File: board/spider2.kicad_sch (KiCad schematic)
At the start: 100 parts, among them J1 NRJ6HH, J10 PJ-320A, J11 PJ359, J12 PJ359, J13 PJ359, J14 PJ359, J15 PJ359, J16 PJ359, J19 PJ359, J2 NRJ6HH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

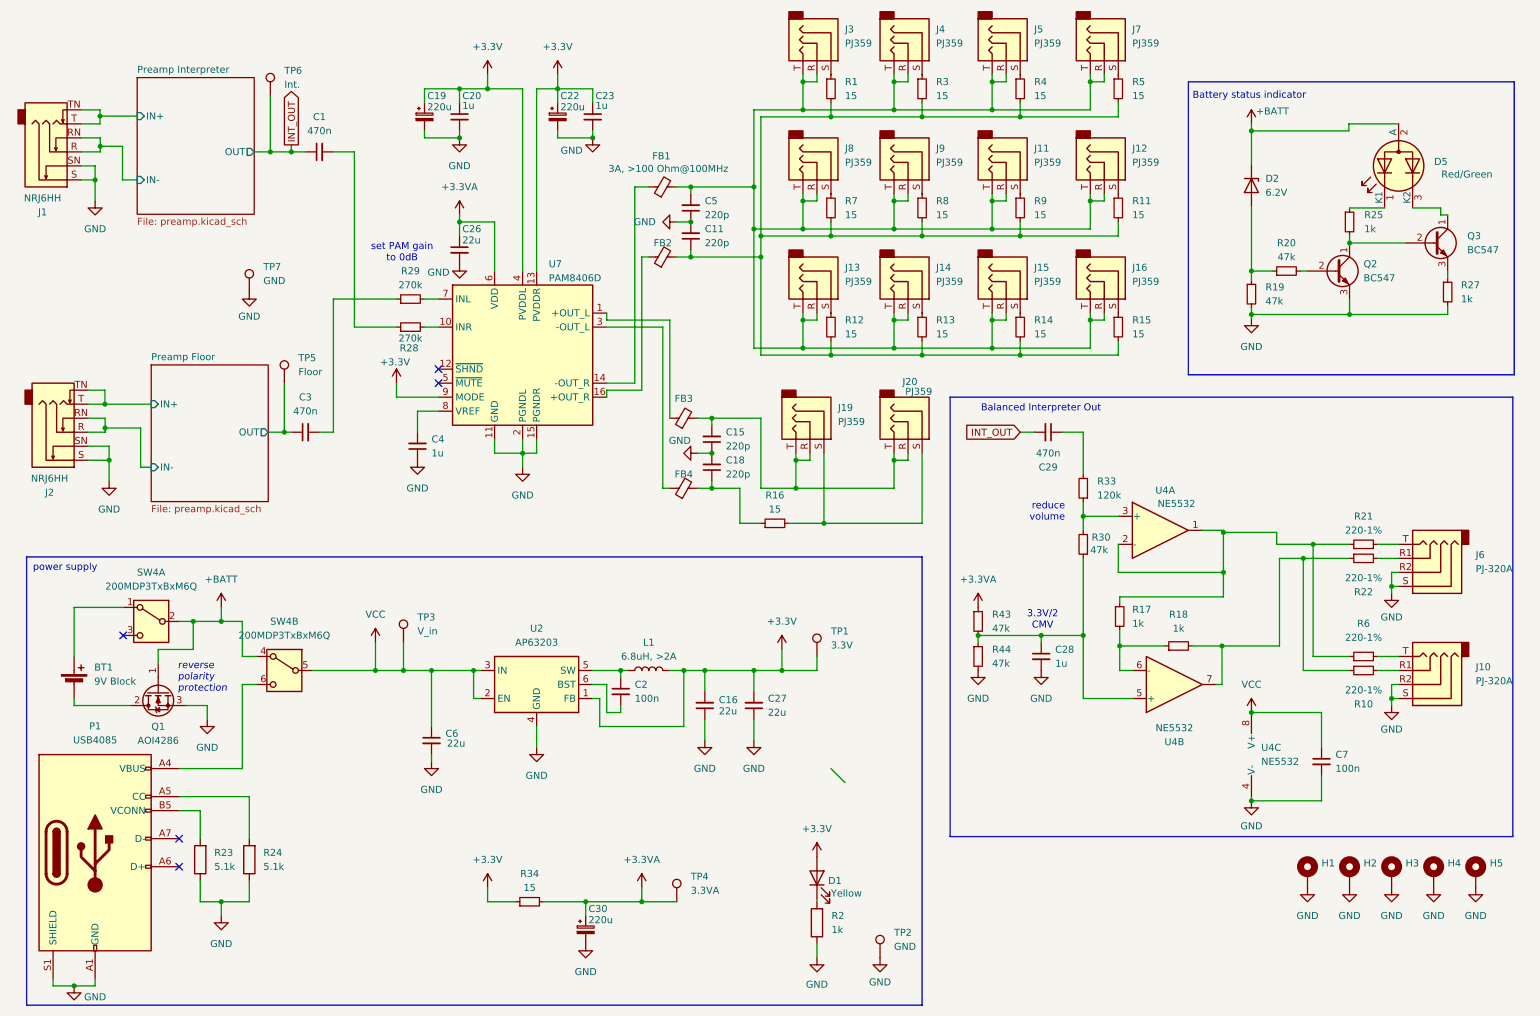
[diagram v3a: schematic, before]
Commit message: reduce BOM and more mechanical stable PJ358
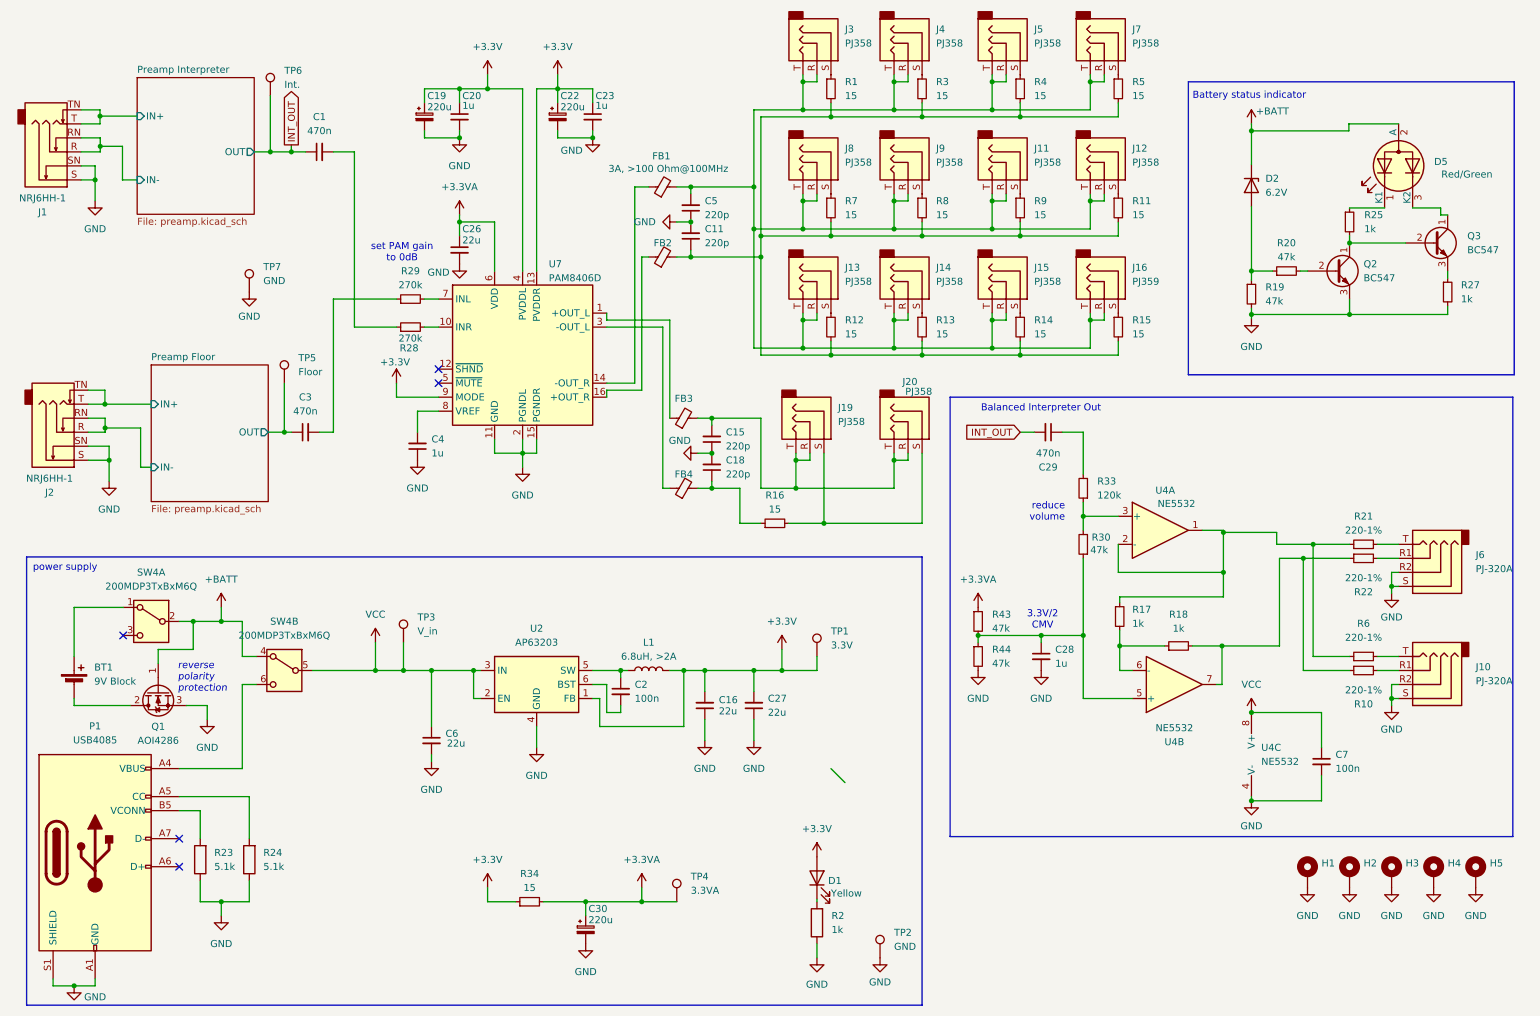
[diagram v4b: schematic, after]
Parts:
- J1, J2: value NRJ6HH -> NRJ6HH-1
- J11, J12, J13, J14, J15, J19, J20, J3, J4, J5, J7, J8, J9: value PJ359 -> PJ358
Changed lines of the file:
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@@
 			)
 		)
-		(property "Value" "PJ359"
+		(property "Value" "PJ358"
 			(at 162.56 64.1349 90)
 			(effects
@@
 			)
 		)
-		(property "Value" "PJ359"
+		(property "Value" "PJ358"
 			(at 162.56 20.9549 90)
 			(effects
@@
 			)
 		)
-		(property "Value" "PJ359"
+		(property "Value" "PJ358"
 			(at 214.63 20.9549 90)
 			(effects
@@
 			)
 		)
-		(property "Value" "PJ359"
+		(property "Value" "PJ358"
 			(at 196.85 64.1349 90)
 			(effects
@@
 			)
 		)
-		(property "Value" "PJ359"
+		(property "Value" "PJ358"
 			(at 161.29 89.5349 90)
 			(effects
@@
 			)
 		)
-		(property "Value" "PJ359"
+		(property "Value" "PJ358"
 			(at 196.85 42.5449 90)
 			(effects
@@
 			)
 		)
-		(property "Value" "NRJ6HH"
+		(property "Value" "NRJ6HH-1"
 			(at 18.415 99.822 0)
 			(effects
@@
 			)
 		)
-		(property "Value" "PJ359"
+		(property "Value" "PJ358"
 			(at 179.07 20.9549 90)
 			(effects
@@
 			)
 		)
-		(property "Value" "PJ359"
+		(property "Value" "PJ358"
 			(at 173.482 84.074 90)
 			(effects
@@
 			)
 		)
-		(property "Value" "NRJ6HH"
+		(property "Value" "NRJ6HH-1"
 			(at 17.145 49.022 0)
 			(effects
@@
 			)
 		)
-		(property "Value" "PJ359"
+		(property "Value" "PJ358"
 			(at 214.63 42.5449 90)
 			(effects
@@
 			)
 		)
-		(property "Value" "PJ359"
+		(property "Value" "PJ358"
 			(at 179.07 42.5449 90)
 			(effects
@@
 			)
 		)
-		(property "Value" "PJ359"
+		(property "Value" "PJ358"
 			(at 196.85 20.9549 90)
 			(effects
@@
 			)
 		)
-		(property "Value" "PJ359"
+		(property "Value" "PJ358"
 			(at 162.56 42.5449 90)
 			(effects
@@
 			)
 		)
-		(property "Value" "PJ359"
+		(property "Value" "PJ358"
 			(at 179.07 64.1349 90)
 			(effects

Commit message: incoorperate matthias feedback
- clearances
- opamp swap
- shorter traces
- ...
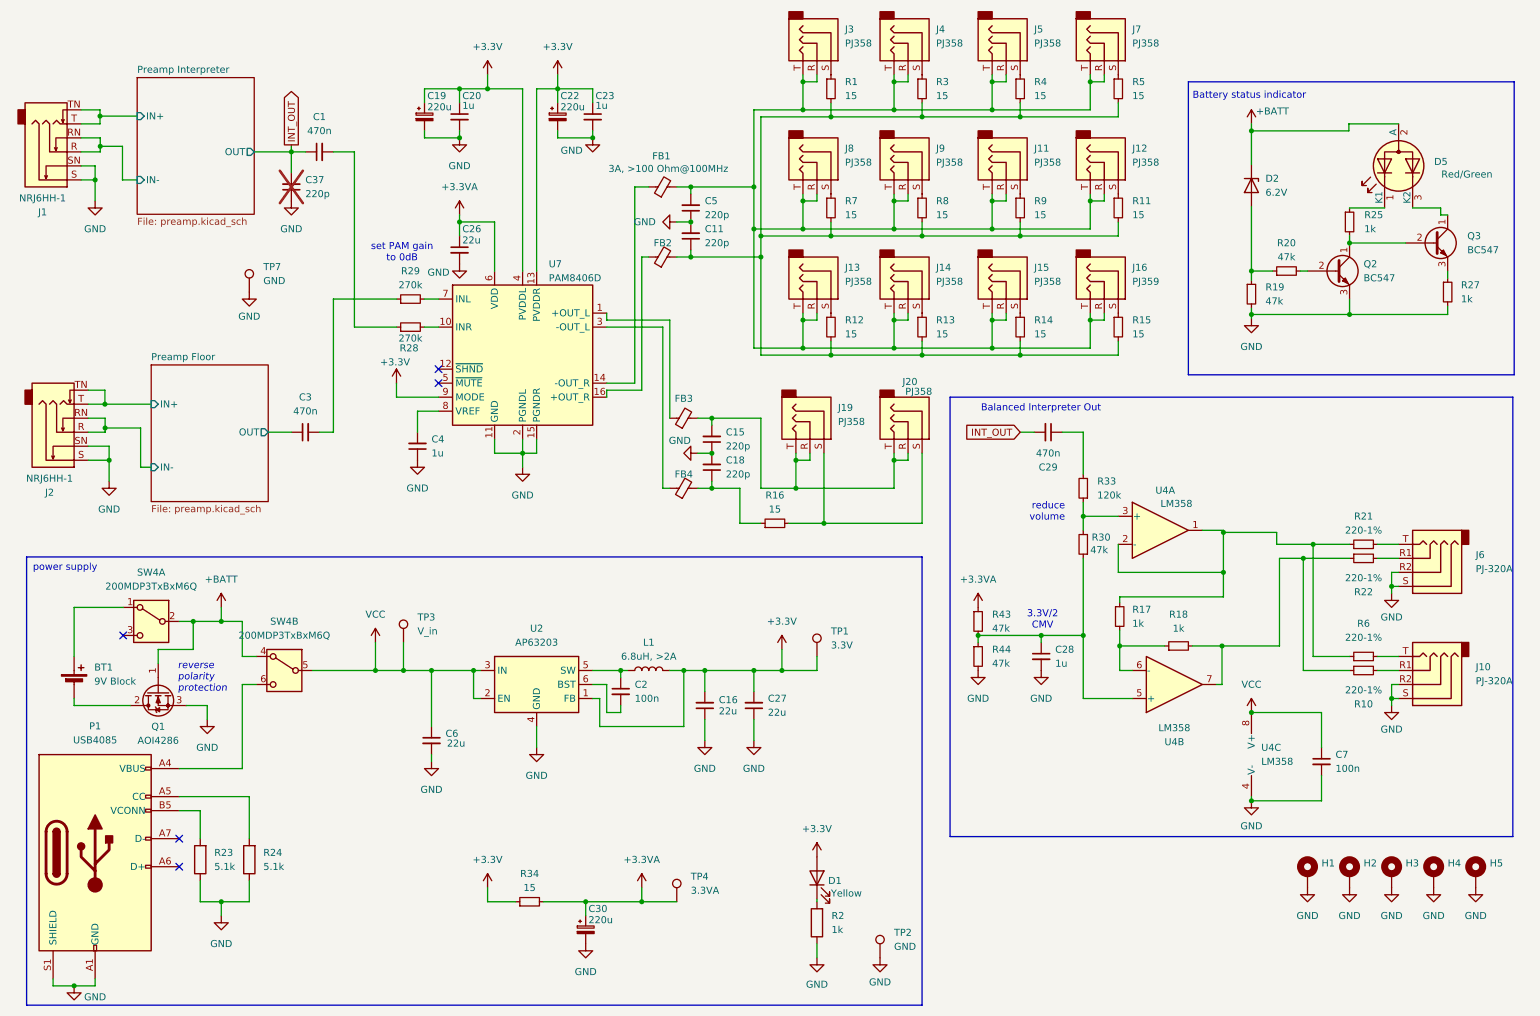
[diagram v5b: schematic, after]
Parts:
- removed TP5: Floor, TestPoint:TestPoint_THTPad_3.0x3.0mm_Drill1.5mm, symbol Connector:TestPoint
- removed TP6: Int., TestPoint:TestPoint_THTPad_3.0x3.0mm_Drill1.5mm, symbol Connector:TestPoint
- added C37: 220p, Capacitor_THT:C_Disc_D3.0mm_W2.0mm_P2.50mm, symbol Device:C_Small
- U4: value NE5532 -> LM358
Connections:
- net GND: now also C37.1
- net INT_OUT: now also C37.2

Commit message: minor changes (silkscreen, etc.)
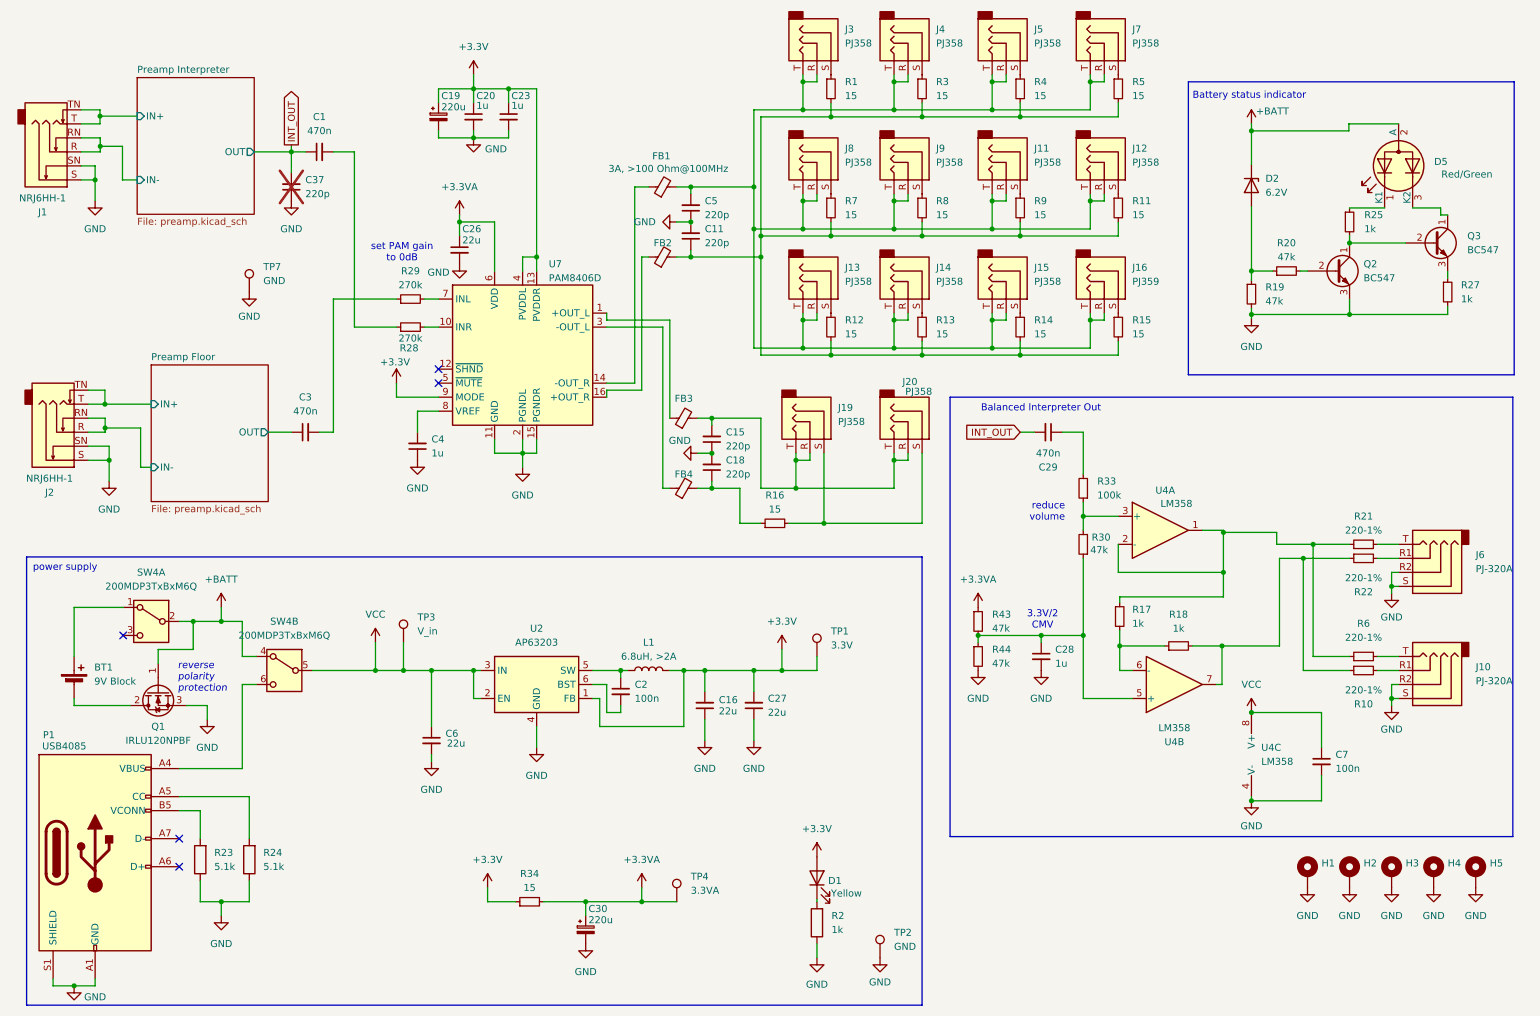
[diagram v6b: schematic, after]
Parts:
- removed C22: 220u, Capacitor_THT:CP_Radial_D6.3mm_P2.50mm, symbol Device:C_Polarized_Small
- Q1: value AOI4286 -> IRLU120NPBF
- R33: value 120k -> 100k
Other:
- moved on the sheet: C19, C20, C23

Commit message: last changes for 0.2 (testpoints, spare footprints,...)
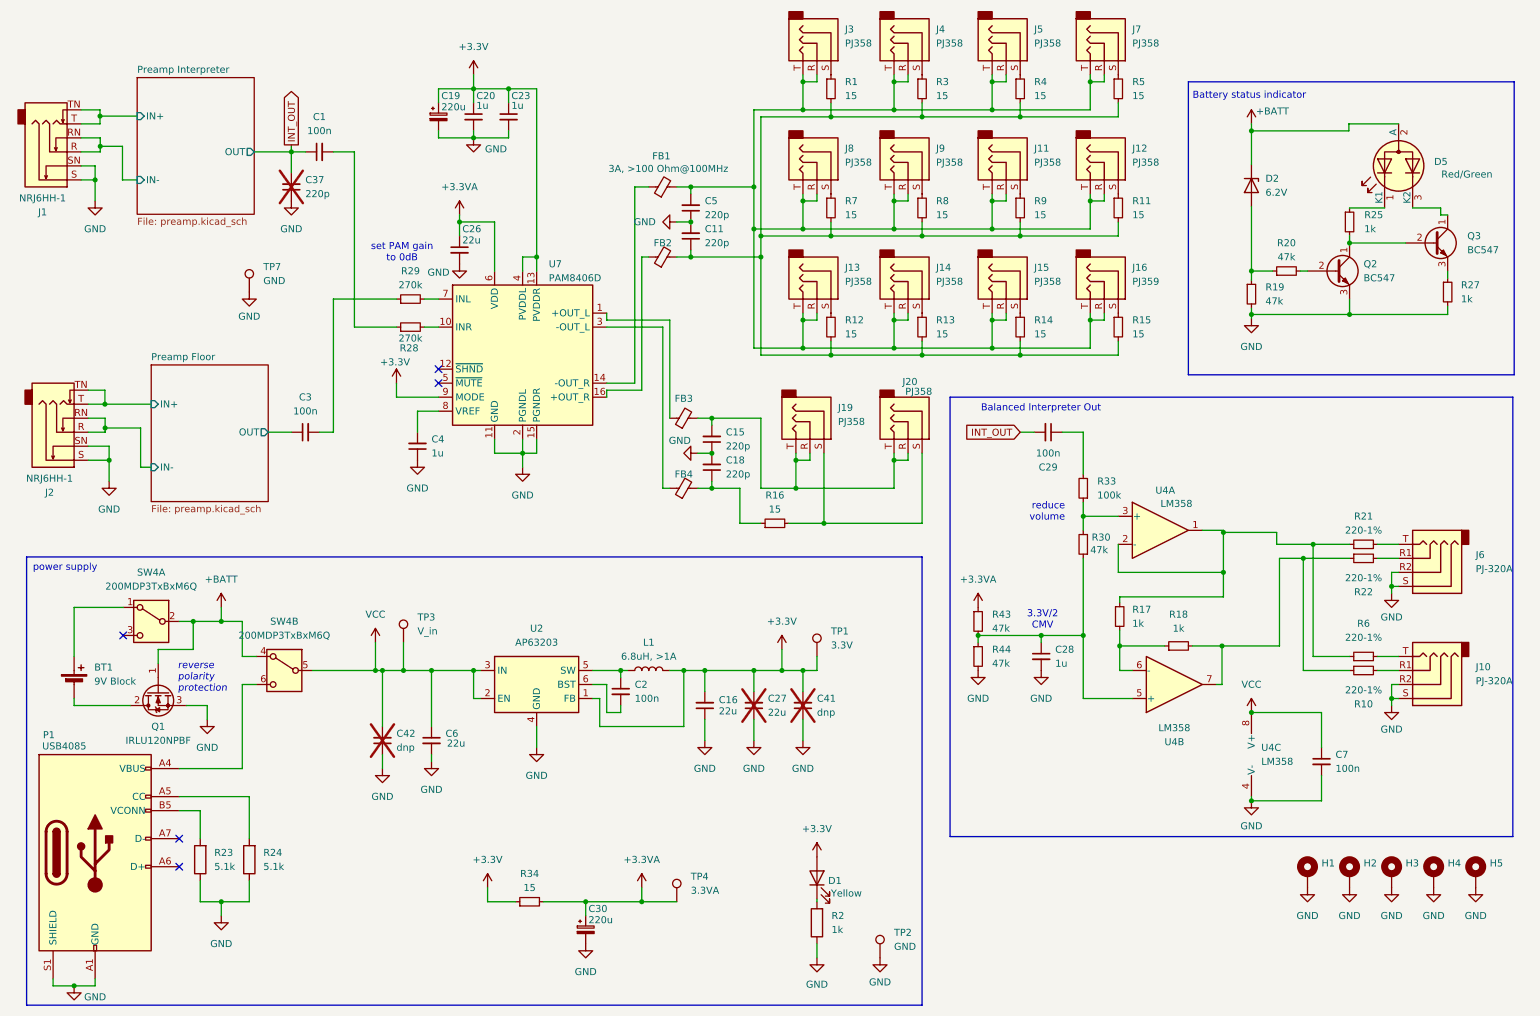
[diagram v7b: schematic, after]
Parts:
- added C41, C42: dnp, Capacitor_THT:C_Disc_D4.3mm_W1.9mm_P5.00mm, symbol Device:C_Small
- C1, C29, C3: value 470n -> 100n
- C27: now not fitted; now left out of the parts list
- L1: value 6.8uH, >2A -> 6.8uH, >1A
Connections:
- net +3.3V: now also C41.2
- net GND: now also C41.1, C42.1
- net VCC: now also C42.2

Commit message: 0.2-prototype
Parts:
- C1, C29, C3: footprint Capacitor_THT:C_Disc_D5.1mm_W3.2mm_P5.00mm -> Capacitor_THT:C_Disc_D4.3mm_W1.9mm_P5.00mm
- J16: value PJ359 -> PJ358
- R28, R29: footprint Resistor_THT:R_Axial_DIN0207_L6.3mm_D2.5mm_P10.16mm_Horizontal -> Resistor_THT:R_Axial_DIN0207_L6.3mm_D2.5mm_P7.62mm_Horizontal
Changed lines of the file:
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@@
 			)
 		)
-		(property "Footprint" "Resistor_THT:R_Axial_DIN0207_L6.3mm_D2.5mm_P10.16mm_Horizontal"
+		(property "Footprint" "Resistor_THT:R_Axial_DIN0207_L6.3mm_D2.5mm_P7.62mm_Horizontal"
 			(at 83.82 67.31 0)
 			(effects
@@
 			)
 		)
-		(property "Footprint" "Resistor_THT:R_Axial_DIN0207_L6.3mm_D2.5mm_P10.16mm_Horizontal"
+		(property "Footprint" "Resistor_THT:R_Axial_DIN0207_L6.3mm_D2.5mm_P7.62mm_Horizontal"
 			(at 83.82 72.39 0)
 			(effects
@@
 			)
 		)
-		(property "Footprint" "Capacitor_THT:C_Disc_D5.1mm_W3.2mm_P5.00mm"
+		(property "Footprint" "Capacitor_THT:C_Disc_D4.3mm_W1.9mm_P5.00mm"
 			(at 199.39 91.44 0)
 			(effects
@@
 			)
 		)
-		(property "Footprint" "Capacitor_THT:C_Disc_D5.1mm_W3.2mm_P5.00mm"
+		(property "Footprint" "Capacitor_THT:C_Disc_D4.3mm_W1.9mm_P5.00mm"
 			(at 67.31 40.64 0)
 			(effects
@@
 			)
 		)
-		(property "Value" "PJ359"
+		(property "Value" "PJ358"
 			(at 214.63 64.1349 90)
 			(effects
@@
 			)
 		)
-		(property "Footprint" "Capacitor_THT:C_Disc_D5.1mm_W3.2mm_P5.00mm"
+		(property "Footprint" "Capacitor_THT:C_Disc_D4.3mm_W1.9mm_P5.00mm"
 			(at 64.77 91.44 0)
 			(effects
